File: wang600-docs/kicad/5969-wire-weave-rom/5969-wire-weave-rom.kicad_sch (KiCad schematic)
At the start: 39 parts, among them Q32 , Q33 , Q34 , U11 7426, U36 SP380A, U38 74LS04

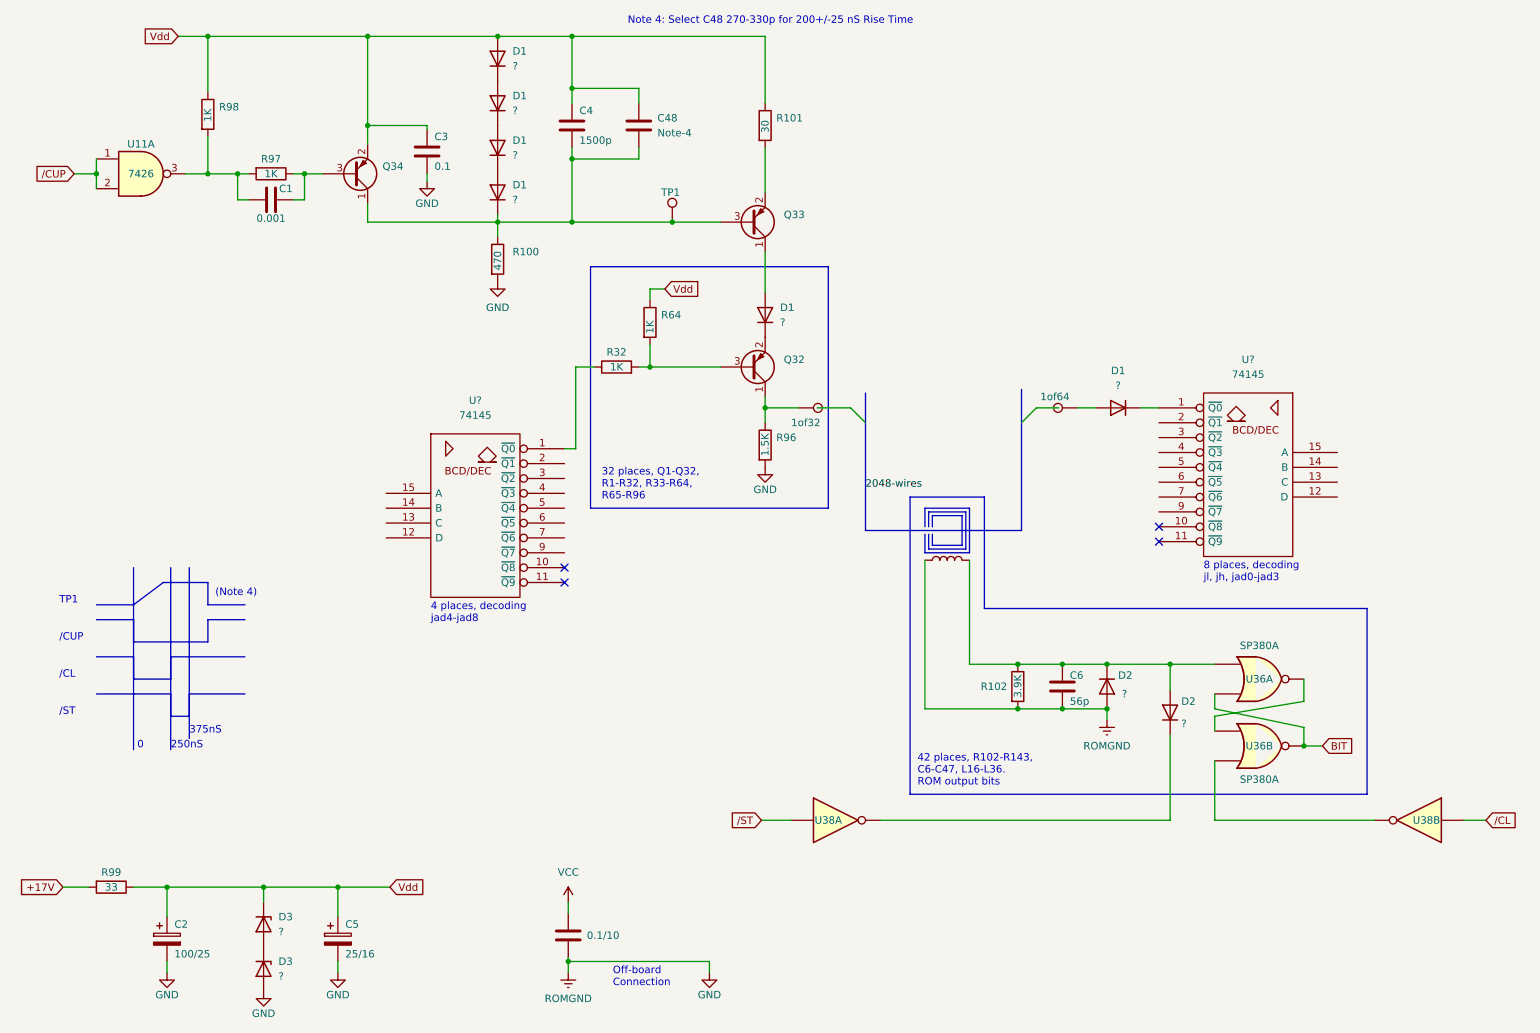
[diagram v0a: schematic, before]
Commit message: add partno xref, more detail to schematics
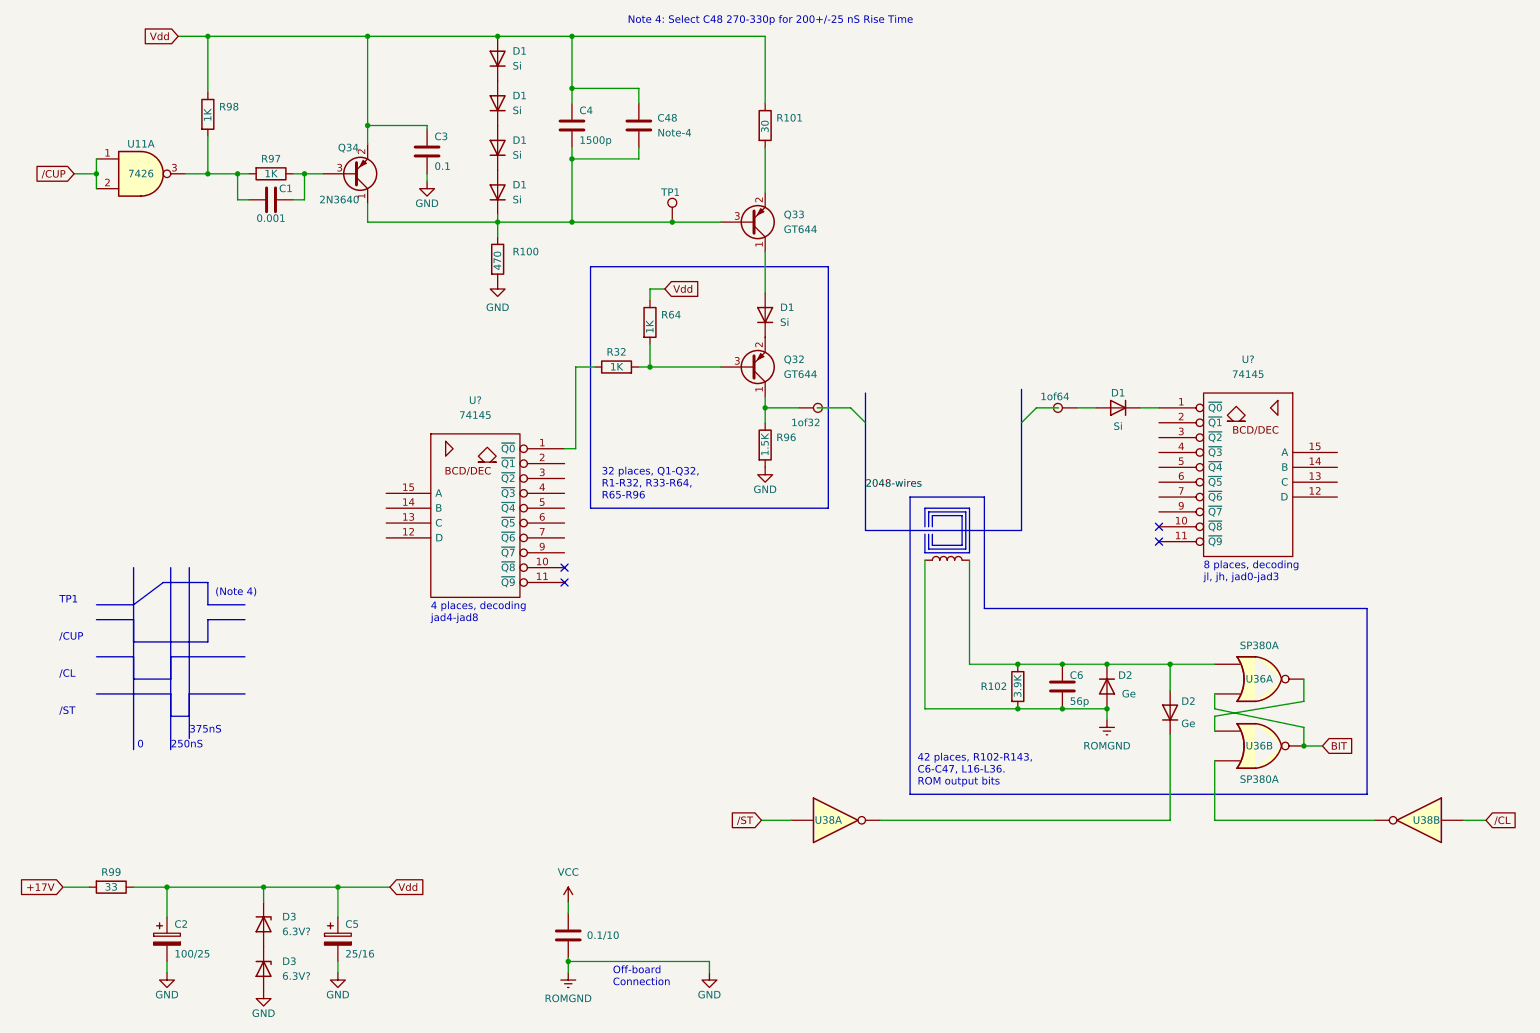
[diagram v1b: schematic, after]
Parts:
- D1: value ? -> Si
- D2: value ? -> Ge
- D3: value ? -> 6.3V?
- Q32, Q33: value (none) -> GT644
- Q34: value (none) -> 2N3640
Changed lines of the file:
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@@
       (effects (font (size 1.27 1.27)) (justify right))
     )
-    (property "Value" "?" (id 1) (at 217.17 140.97 90)
+    (property "Value" "Ge" (id 1) (at 217.17 140.97 90)
       (effects (font (size 1.27 1.27)) (justify right))
     )
@@
       (effects (font (size 1.27 1.27)) (justify left))
     )
-    (property "Value" " " (id 1) (at 149.225 56.5149 0)
+    (property "Value" "GT644" (id 1) (at 149.225 56.5149 0)
       (effects (font (size 1.27 1.27)) (justify left))
     )
@@
       (effects (font (size 1.27 1.27)) (justify right))
     )
-    (property "Value" "?" (id 1) (at 102.87 36.1949 90)
+    (property "Value" "Si" (id 1) (at 102.87 36.1949 90)
       (effects (font (size 1.27 1.27)) (justify right))
     )
@@
       (effects (font (size 1.27 1.27)) (justify left))
     )
-    (property "Value" "?" (id 1) (at 207.01 135.8899 90)
+    (property "Value" "Ge" (id 1) (at 207.01 135.8899 90)
       (effects (font (size 1.27 1.27)) (justify left))
     )
@@
       (effects (font (size 1.27 1.27)) (justify right))
     )
-    (property "Value" "?" (id 1) (at 148.59 72.3899 90)
+    (property "Value" "Si" (id 1) (at 148.59 72.3899 90)
       (effects (font (size 1.27 1.27)) (justify right))
     )
@@
   )
   (symbol (lib_id "Device:Q_PNP_CEB") (at 75.565 46.99 0) (mirror x) (unit 1)
-    (in_bom yes) (on_board yes) (fields_autoplaced)
-    (property "Reference" "Q34" (id 0) (at 80.645 45.7199 0)
-      (effects (font (size 1.27 1.27)) (justify left))
-    )
-    (property "Value" " " (id 1) (at 80.645 48.2599 0)
+    (in_bom yes) (on_board yes)
+    (property "Reference" "Q34" (id 0) (at 73.025 42.545 0)
+      (effects (font (size 1.27 1.27)) (justify left))
+    )
+    (property "Value" "2N3640" (id 1) (at 69.85 51.435 0)
       (effects (font (size 1.27 1.27)) (justify left))
     )
@@
   (symbol (lib_id "Device:D_Zener") (at 60.325 175.26 270) (unit 1)
     (in_bom yes) (on_board yes) (fields_autoplaced)
-    (property "Reference" "D3" (id 0) (at 62.865 173.9899 90)
-      (effects (font (size 1.27 1.27)) (justify left))
-    )
-    (property "Value" "?" (id 1) (at 62.865 176.5299 90)
+    (property "Reference" "D3" (id 0) (at 63.5 173.9899 90)
+      (effects (font (size 1.27 1.27)) (justify left))
+    )
+    (property "Value" "6.3V?" (id 1) (at 63.5 176.5299 90)
       (effects (font (size 1.27 1.27)) (justify left))
     )
@@
       (effects (font (size 1.27 1.27)) (justify right))
     )
-    (property "Value" "?" (id 1) (at 102.87 43.8149 90)
+    (property "Value" "Si" (id 1) (at 102.87 43.8149 90)
       (effects (font (size 1.27 1.27)) (justify right))
     )
@@
   (symbol (lib_id "Device:D_Zener") (at 60.325 182.88 270) (unit 1)
     (in_bom yes) (on_board yes) (fields_autoplaced)
-    (property "Reference" "D3" (id 0) (at 62.865 181.6099 90)
-      (effects (font (size 1.27 1.27)) (justify left))
-    )
-    (property "Value" "?" (id 1) (at 62.865 184.1499 90)
+    (property "Reference" "D3" (id 0) (at 63.5 181.6099 90)
+      (effects (font (size 1.27 1.27)) (justify left))
+    )
+    (property "Value" "6.3V?" (id 1) (at 63.5 184.1499 90)
       (effects (font (size 1.27 1.27)) (justify left))
     )
@@
       (effects (font (size 1.27 1.27)) (justify right))
     )
-    (property "Value" "?" (id 1) (at 102.87 51.4349 90)
+    (property "Value" "Si" (id 1) (at 102.87 51.4349 90)
       (effects (font (size 1.27 1.27)) (justify right))
     )
@@
   )
   (symbol (lib_id "Device:D") (at 206.375 86.995 180) (unit 1)
-    (in_bom yes) (on_board yes) (fields_autoplaced)
-    (property "Reference" "D1" (id 0) (at 206.375 80.645 0))
-    (property "Value" "?" (id 1) (at 206.375 83.185 0))
+    (in_bom yes) (on_board yes)
+    (property "Reference" "D1" (id 0) (at 206.375 84.455 0))
+    (property "Value" "Si" (id 1) (at 206.375 90.17 0))
     (property "Footprint" "" (id 2) (at 206.375 86.995 0)
       (effects (font (size 1.27 1.27)) hide)
@@
       (effects (font (size 1.27 1.27)) (justify right))
     )
-    (property "Value" "?" (id 1) (at 102.87 28.5749 90)
+    (property "Value" "Si" (id 1) (at 102.87 28.5749 90)
       (effects (font (size 1.27 1.27)) (justify right))
     )
@@
       (effects (font (size 1.27 1.27)) (justify left))
     )
-    (property "Value" " " (id 1) (at 149.225 81.2799 0)
+    (property "Value" "GT644" (id 1) (at 149.225 81.2799 0)
       (effects (font (size 1.27 1.27)) (justify left))
     )
@@
     )
     (path "/4a5dbbcd-d4bc-428b-8a92-ca85144088c9"
-      (reference "D1") (unit 1) (value "?") (footprint "")
+      (reference "D1") (unit 1) (value "Si") (footprint "")
     )
     (path "/777946ac-1b34-465f-8bc1-2feacf1d8311"
-      (reference "D1") (unit 1) (value "?") (footprint "")
+      (reference "D1") (unit 1) (value "Si") (footprint "")
     )
     (path "/9038e698-e3a3-4d55-b4de-ef5852b59874"
-      (reference "D1") (unit 1) (value "?") (footprint "")
+      (reference "D1") (unit 1) (value "Si") (footprint "")
     )
     (path "/aeb96825-7f18-43dd-a670-d19d51ba1f14"
-      (reference "D1") (unit 1) (value "?") (footprint "")
+      (reference "D1") (unit 1) (value "Si") (footprint "")
     )
     (path "/ccf1a0f4-1090-47ba-899c-d3f2ed02461a"
-      (reference "D1") (unit 1) (value "?") (footprint "")
+      (reference "D1") (unit 1) (value "Si") (footprint "")
     )
     (path "/d89c71a7-2bfc-491c-bbe1-aa4a15a93355"
-      (reference "D1") (unit 1) (value "?") (footprint "")
+      (reference "D1") (unit 1) (value "Si") (footprint "")
     )
     (path "/0aabac83-ad7e-4a06-8e3b-57b1f8711b48"
-      (reference "D2") (unit 1) (value "?") (footprint "")
+      (reference "D2") (unit 1) (value "Ge") (footprint "")
     )
     (path "/658f84a3-34bc-4bb1-8298-f71b3556ad37"
-      (reference "D2") (unit 1) (value "?") (footprint "")
+      (reference "D2") (unit 1) (value "Ge") (footprint "")
     )
     (path "/8641a531-5e33-48cc-9899-4d8bb6a777be"
-      (reference "D3") (unit 1) (value "?") (footprint "")
+      (reference "D3") (unit 1) (value "6.3V?") (footprint "")
     )
     (path "/97af5f3c-7326-41b4-9624-573ed826ebbe"
-      (reference "D3") (unit 1) (value "?") (footprint "")
+      (reference "D3") (unit 1) (value "6.3V?") (footprint "")
     )
     (path "/ff2fd7d1-a26d-4a68-ba45-eff7d8190762"
@@
     )
     (path "/fa730bff-7ae7-4cfc-aa0b-6b723ed31b48"
-      (reference "Q32") (unit 1) (value " ") (footprint "")
+      (reference "Q32") (unit 1) (value "GT644") (footprint "")
     )
     (path "/18b6dcb6-5ab3-481b-b998-33e8cf6d281f"
-      (reference "Q33") (unit 1) (value " ") (footprint "")
+      (reference "Q33") (unit 1) (value "GT644") (footprint "")
     )
     (path "/7bbf981c-a063-4e30-8911-e4228e1c0743"
-      (reference "Q34") (unit 1) (value " ") (footprint "")
+      (reference "Q34") (unit 1) (value "2N3640") (footprint "")
     )
     (path "/acd09e9c-71b1-44b1-b4b1-7e32d519f348"

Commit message: cleanup schematics
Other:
- moved on the sheet: C3, C5, D3

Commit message: yet more schematic cleanup
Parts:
- removed TP1: TestPoint, symbol Connector:TestPoint
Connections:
- net energize: now reaches C4.2, C48.2, D1.1 (K), Q33.3 (B), Q34.1 (C), R100.1
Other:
- note added: "energize"
- note removed: "TP1"
- title: (none) -> Wang 500/600 Wire-Weave ROM
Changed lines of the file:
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@@
 (kicad_sch (version 20211123) (generator eeschema)
   (paper "A4")
-  (junction (at 130.175 55.245) (diameter 0) (color 0 0 0 0)
+  (title_block
+    (title "Wang 500/600 Wire-Weave ROM")
+    (date "2024-04-15")
+  )
+  (junction (at 125.095 55.245) (diameter 0) (color 0 0 0 0)
   )
   (junction (at 238.125 144.78) (diameter 0) (color 0 0 0 0)
@@
     (stroke (width 0) (type default) (color 0 0 0 0))
   )
-  (polyline (pts (xy 31.75 123.19) (xy 38.1 123.19))
+  (polyline (pts (xy 31.75 116.84) (xy 38.1 116.84))
     (stroke (width 0) (type solid) (color 0 0 0 1))
   )
@@
     (stroke (width 0) (type default) (color 0 0 0 0))
   )
-  (polyline (pts (xy 38.1 120.65) (xy 43.18 116.84))
-    (stroke (width 0) (type solid) (color 0 0 0 1))
-  )
   (wire (pts (xy 126.365 68.58) (xy 126.365 66.675))
     (stroke (width 0) (type default) (color 0 0 0 0))
@@
     (stroke (width 0) (type default) (color 0 0 0 0))
   )
+  (polyline (pts (xy 31.75 127) (xy 38.1 127))
+    (stroke (width 0) (type solid) (color 0 0 0 1))
+  )
   (wire (pts (xy 26.035 168.91) (xy 30.48 168.91))
     (stroke (width 0) (type default) (color 0 0 0 0))
@@
   (wire (pts (xy 238.125 137.16) (xy 238.125 133.35))
     (stroke (width 0) (type default) (color 0 0 0 0))
+  )
+  (polyline (pts (xy 43.18 123.19) (xy 50.8 123.19))
+    (stroke (width 0) (type solid) (color 0 0 0 1))
   )
   (wire (pts (xy 165.735 157.48) (xy 215.265 157.48))
@@
     (stroke (width 0) (type default) (color 0 0 0 0))
   )
-  (polyline (pts (xy 38.1 127) (xy 50.8 127))
+  (polyline (pts (xy 38.1 120.65) (xy 50.8 120.65))
     (stroke (width 0) (type solid) (color 0 0 0 1))
   )
@@
     (stroke (width 0) (type default) (color 0 0 0 0))
   )
-  (polyline (pts (xy 50.8 120.65) (xy 57.15 120.65))
-    (stroke (width 0) (type solid) (color 0 0 0 1))
-  )
   (wire (pts (xy 145.415 157.48) (xy 150.495 157.48))
     (stroke (width 0) (type default) (color 0 0 0 0))
   )
-  (polyline (pts (xy 50.8 127) (xy 50.8 123.19))
+  (polyline (pts (xy 50.8 120.65) (xy 50.8 116.84))
     (stroke (width 0) (type solid) (color 0 0 0 1))
   )
@@
     (stroke (width 0) (type default) (color 0 0 0 0))
   )
-  (polyline (pts (xy 43.18 116.84) (xy 50.8 116.84))
-    (stroke (width 0) (type solid) (color 0 0 0 1))
-  )
   (wire (pts (xy 222.885 147.32) (xy 222.885 157.48))
     (stroke (width 0) (type default) (color 0 0 0 0))
@@
     (stroke (width 0) (type default) (color 0 0 0 0))
   )
-  (polyline (pts (xy 50.8 123.19) (xy 57.15 123.19))
-    (stroke (width 0) (type solid) (color 0 0 0 1))
-  )
-  (polyline (pts (xy 38.1 123.19) (xy 38.1 127))
+  (polyline (pts (xy 50.8 116.84) (xy 57.15 116.84))
+    (stroke (width 0) (type solid) (color 0 0 0 1))
+  )
+  (polyline (pts (xy 38.1 116.84) (xy 38.1 120.65))
     (stroke (width 0) (type solid) (color 0 0 0 1))
   )
@@
     (stroke (width 0) (type default) (color 0 0 0 0))
   )
+  (polyline (pts (xy 50.8 123.19) (xy 50.8 127))
+    (stroke (width 0) (type solid) (color 0 0 0 1))
+  )
   (wire (pts (xy 146.05 34.925) (xy 146.05 23.495))
     (stroke (width 0) (type default) (color 0 0 0 0))
@@
   )
   (wire (pts (xy 50.8 23.495) (xy 50.8 33.02))
+    (stroke (width 0) (type default) (color 0 0 0 0))
+  )
+  (wire (pts (xy 125.095 55.245) (xy 138.43 55.245))
     (stroke (width 0) (type default) (color 0 0 0 0))
   )
@@
     (stroke (width 0) (type default) (color 0 0 0 0))
   )
-  (polyline (pts (xy 50.8 116.84) (xy 50.8 120.65))
-    (stroke (width 0) (type solid) (color 0 0 0 1))
-  )
-  (wire (pts (xy 130.175 55.245) (xy 138.43 55.245))
-    (stroke (width 0) (type default) (color 0 0 0 0))
-  )
   (wire (pts (xy 222.885 139.7) (xy 238.125 137.16))
     (stroke (width 0) (type default) (color 0 0 0 0))
@@
     (stroke (width 0) (type solid) (color 0 0 0 1))
   )
+  (wire (pts (xy 125.095 49.53) (xy 125.095 55.245))
+    (stroke (width 0) (type default) (color 0 0 0 0))
+  )
   (polyline (pts (xy 156.845 104.14) (xy 156.845 62.865))
     (stroke (width 0) (type default) (color 0 0 0 0))
@@
     (stroke (width 0) (type default) (color 204 102 0 1))
   )
+  (wire (pts (xy 127 49.53) (xy 125.095 49.53))
+    (stroke (width 0) (type default) (color 0 0 0 0))
+  )
   (wire (pts (xy 112.395 171.45) (xy 112.395 173.355))
     (stroke (width 0) (type default) (color 0 0 0 0))
@@
     (stroke (width 0) (type default) (color 0 0 0 0))
   )
+  (polyline (pts (xy 50.8 127) (xy 57.15 127))
+    (stroke (width 0) (type solid) (color 0 0 0 1))
+  )
   (wire (pts (xy 55.88 51.435) (xy 55.88 46.99))
     (stroke (width 0) (type default) (color 0 0 0 0))
@@
     (stroke (width 0) (type default) (color 204 102 0 1))
   )
-  (polyline (pts (xy 31.75 120.65) (xy 38.1 120.65))
-    (stroke (width 0) (type solid) (color 0 0 0 1))
-  )
   (wire (pts (xy 65.405 46.99) (xy 67.31 46.99))
     (stroke (width 0) (type default) (color 0 0 0 0))
@@
     (stroke (width 0) (type default) (color 0 0 0 0))
   )
-  (wire (pts (xy 113.03 55.245) (xy 130.175 55.245))
-    (stroke (width 0) (type default) (color 0 0 0 0))
+  (wire (pts (xy 113.03 55.245) (xy 125.095 55.245))
+    (stroke (width 0) (type default) (color 0 0 0 0))
+  )
+  (polyline (pts (xy 38.1 127) (xy 43.18 123.19))
+    (stroke (width 0) (type solid) (color 0 0 0 1))
   )
   (polyline (pts (xy 38.1 114.3) (xy 38.1 145.415))
@@
   )
   (text "250nS" (at 44.45 145.415 0)
+    (effects (font (size 1.27 1.27)) (justify left bottom))
+  )
+  (text "(Note 4)" (at 52.07 125.73 0)
     (effects (font (size 1.27 1.27)) (justify left bottom))
   )
@@
     (effects (font (size 1.27 1.27)) (justify left bottom))
   )
-  (text "(Note 4)" (at 52.07 119.38 0)
-    (effects (font (size 1.27 1.27)) (justify left bottom))
-  )
   (text "Note 4: Select C48 270-330p for 200+/-25 nS Rise Time"
     (at 122.555 21.59 0)
     (effects (font (size 1.27 1.27)) (justify left bottom))
   )
-  (text "/CUP" (at 25.4 127 0)
-    (effects (font (size 1.27 1.27)) (justify left bottom))
-  )
-  (text "/ST" (at 25.4 139.7 0)
-    (effects (font (size 1.27 1.27)) (justify left bottom))
+  (text "/CUP" (at 31.75 120.65 180)
+    (effects (font (size 1.27 1.27)) (justify right bottom))
+  )
+  (text "/ST" (at 31.75 139.7 180)
+    (effects (font (size 1.27 1.27)) (justify right bottom))
   )
   (text "8 places, decoding\njl, jh, jad0-jad3" (at 220.98 116.84 0)
@@
     (effects (font (size 1.27 1.27)) (justify left bottom))
   )
-  (text "/CL" (at 25.4 133.35 0)
-    (effects (font (size 1.27 1.27)) (justify left bottom))
+  (text "/CL" (at 31.75 133.35 180)
+    (effects (font (size 1.27 1.27)) (justify right bottom))
   )
   (text "375nS" (at 47.625 142.875 0)
     (effects (font (size 1.27 1.27)) (justify left bottom))
   )
-  (text "TP1" (at 25.4 120.65 0)
-    (effects (font (size 1.27 1.27)) (justify left bottom))
+  (text "energize" (at 31.75 127 180)
+    (effects (font (size 1.27 1.27)) (justify right bottom))
   )
   (text "32 places, Q1-Q32,\nR1-R32, R33-R64,\nR65-R96" (at 118.11 102.87 0)
@@
     (effects (font (size 1.27 1.27)) (justify left))
     (property "Intersheet References" "${INTERSHEET_REFS}" (id 0) (at 275.2817 157.4006 0)
+      (effects (font (size 1.27 1.27)) (justify left) hide)
+    )
+  )
+  (global_label "energize" (shape input) (at 127 49.53 0) (fields_autoplaced)
+    (effects (font (size 1.27 1.27)) (justify left))
+    (property "Intersheet References" "${INTERSHEET_REFS}" (id 0) (at 137.396 49.4506 0)
       (effects (font (size 1.27 1.27)) (justify left) hide)
     )
@@
     (pin "2")
   )
-  (symbol (lib_id "Connector:TestPoint") (at 130.175 55.245 0) (unit 1)
-    (in_bom yes) (on_board yes)
-    (property "Reference" "TP1" (id 0) (at 128.27 50.165 0)
-      (effects (font (size 1.27 1.27)) (justify left))
-    )
-    (property "Value" "TestPoint" (id 1) (at 132.08 53.2129 0)
-      (effects (font (size 1.27 1.27)) (justify left) hide)
-    )
-    (property "Footprint" "" (id 2) (at 135.255 55.245 0)
-      (effects (font (size 1.27 1.27)) hide)
-    )
-    (property "Datasheet" "~" (id 3) (at 135.255 55.245 0)
-      (effects (font (size 1.27 1.27)) hide)
-    )
-    (pin "1")
-  )
   (symbol (lib_name "74LS04_1") (lib_id "74xx:74LS04") (at 158.115 157.48 0) (unit 1)
     (in_bom yes) (on_board yes)
@@
       (reference "ROMGND") (unit 1) (value "GNDREF") (footprint "")
     )
-    (path "/6f47afab-0f52-4a8f-82f1-bde9e0c218ed"
-      (reference "TP1") (unit 1) (value "TestPoint") (footprint "")
-    )
     (path "/f38f084b-aa47-484c-af97-a87d934da924"
